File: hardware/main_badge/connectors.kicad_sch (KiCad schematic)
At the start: 8 parts, among them J10 Micro_SD_Card, J11 Mechanical/Grounds, J12 Mechanical/Grounds, J5 SAO1, J6 SAO2, J7 Conn_01x08_Socket, J8 Conn_01x08_Socket, J9 Conn_ARM_SWD_TagConnect_TC203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

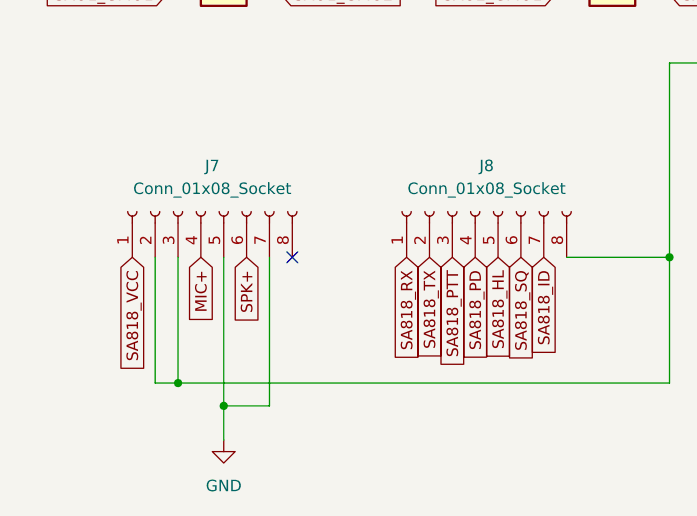
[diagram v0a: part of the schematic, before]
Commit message: connect J7 pin 8 to GND
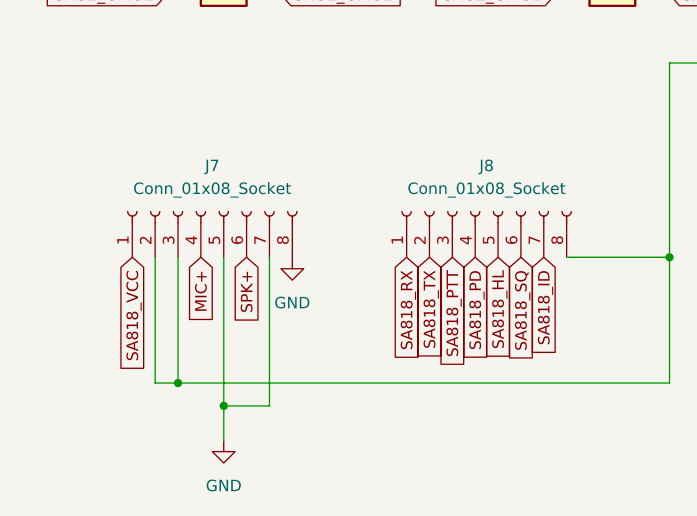
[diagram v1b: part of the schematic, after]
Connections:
- net GND: now also J7.8 (Pin_8)
- no-connect marks 4 -> 3
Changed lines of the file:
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@@
-	)
-	(no_connect
-		(at 52.07 86.36)
 	)
 	(no_connect
@@
 					(unit 1)
 				)
+			)
+		)
+	)
+	(symbol
+		(lib_id "power:GND")
+		(at 52.07 86.36 0)
+		(unit 1)
+		(exclude_from_sim no)
+		(in_bom yes)
+		(on_board yes)
+		(dnp no)
+		(fields_autoplaced yes)
+		(property "Reference" "#PWR019"
+			(at 52.07 92.71 0)
+			(effects
+				(font
+					(size 1.27 1.27)
+				)
+				(hide yes)
+			)
+		)
+		(property "Value" "GND"
+			(at 52.07 91.44 0)
+			(effects
+				(font
+					(size 1.27 1.27)
+				)
+			)
+		)
+		(property "Footprint" ""
+			(at 52.07 86.36 0)
+			(effects
+				(font
+					(size 1.27 1.27)
+				)
+				(hide yes)
+			)
+		)
+		(property "Datasheet" ""
+			(at 52.07 86.36 0)
+			(effects
+				(font
+					(size 1.27 1.27)
+				)
+				(hide yes)
+			)
+		)
+		(property "Description" "Power symbol creates a global label with name \"GND\" , ground"
+			(at 52.07 86.36 0)
+			(effects
+				(font
+					(size 1.27 1.27)
+				)
+				(hide yes)
+			)
+		)
+		(pin "1"
+		)
+		(instances
+			(project ""
+				(path "/6bfeada4-0da3-4bdd-af4a-70929e466b35/7e9c56de-ddef-4aba-ac8d-c699010ce68c"
+					(reference "#PWR019")
+					(unit 1)
+				)
